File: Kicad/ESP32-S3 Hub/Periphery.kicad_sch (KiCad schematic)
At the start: 12 parts, among them SW1 Mitsumi R-667996, SW2 Mitsumi R-667996, SW3 DS04-254-2-04BK-SMT, U2 74HC595, U3 THVD1420DRLR

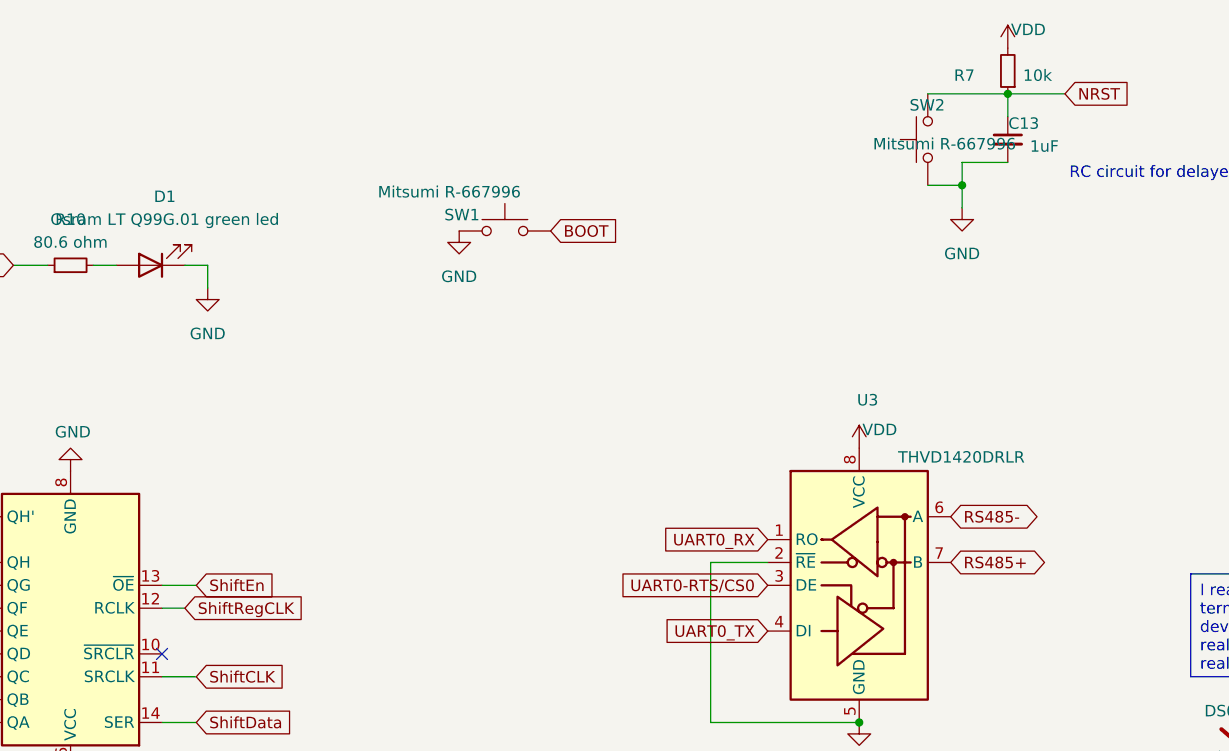
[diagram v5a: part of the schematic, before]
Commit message: Fixed OE pin by adding pullup, updated silkscreen
The silkscreen looks really nice now, I have all the port labels.
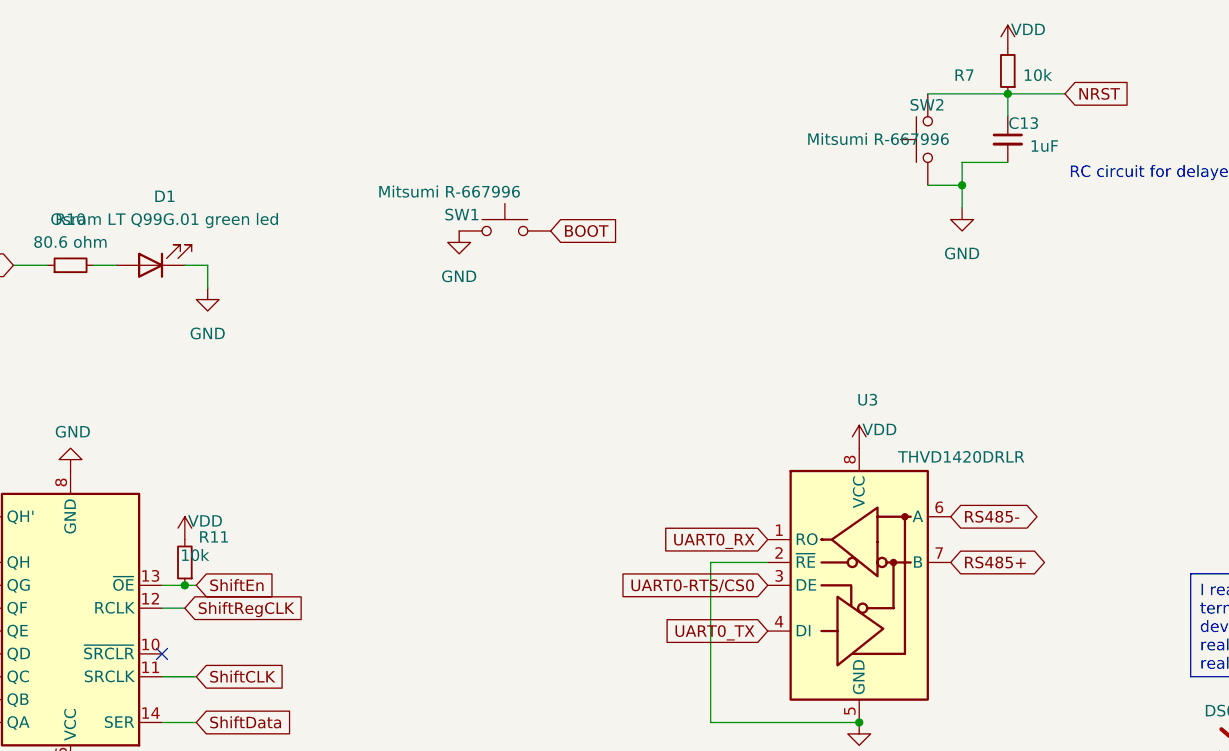
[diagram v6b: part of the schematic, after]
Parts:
- added R11: 10k, Resistor_SMD:R_0402_1005Metric, symbol Device:R_Small
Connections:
- net ShiftEn: now also R11.1
- net VDD: now also R11.2
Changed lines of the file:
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@@
+		(color 0 0 0 0)
+	)
+	(junction
+		(at 69.85 86.36)
+		(diameter 0)
 		(color 0 0 0 0)
 	)
@@
 	(wire
 		(pts
-			(xy 67.31 86.36) (xy 71.12 86.36)
+			(xy 67.31 86.36) (xy 69.85 86.36)
 		)
 		(stroke
@@
 		(pts
 			(xy 72.39 50.8) (xy 72.39 53.34)
+		)
+		(stroke
+			(width 0)
+			(type default)
+		)
+	)
+	(wire
+		(pts
+			(xy 69.85 86.36) (xy 71.12 86.36)
 		)
 		(stroke
@@
 		)
 		(property "Value" "Mitsumi R-667996"
-			(at 146.304 37.338 90)
+			(at 138.938 36.83 90)
 			(effects
 				(font
@@
 	(symbol
 		(lib_id "power:VDD")
+		(at 69.85 81.28 0)
+		(unit 1)
+		(exclude_from_sim no)
+		(in_bom yes)
+		(on_board yes)
+		(dnp no)
+		(property "Reference" "#PWR079"
+			(at 69.85 85.09 0)
+			(effects
+				(font
+					(size 1.27 1.27)
+				)
+				(hide yes)
+			)
+		)
+		(property "Value" "VDD"
+			(at 72.136 79.248 0)
+			(effects
+				(font
+					(size 1.27 1.27)
+				)
+			)
+		)
+		(property "Footprint" ""
+			(at 69.85 81.28 0)
+			(effects
+				(font
+					(size 1.27 1.27)
+				)
+				(hide yes)
+			)
+		)
+		(property "Datasheet" ""
+			(at 69.85 81.28 0)
+			(effects
+				(font
+					(size 1.27 1.27)
+				)
+				(hide yes)
+			)
+		)
+		(property "Description" "Power symbol creates a global label with name \"VDD\""
+			(at 69.85 81.28 0)
+			(effects
+				(font
+					(size 1.27 1.27)
+				)
+				(hide yes)
+			)
+		)
+		(pin "1"
+		)
+		(instances
+			(project "ESP32-S3 Hub"
+				(path "/a8c80fba-3bca-4358-b5bb-9ebf9383c658/c12991ca-4617-4c32-8678-9934d12b2f96"
+					(reference "#PWR079")
+					(unit 1)
+				)
+			)
+		)
+	)
+	(symbol
+		(lib_id "power:VDD")
 		(at 161.29 26.67 0)
 		(unit 1)
@@
 					(unit 1)
 				)
+			)
+		)
+	)
+	(symbol
+		(lib_id "Device:R_Small")
+		(at 69.85 83.82 180)
+		(unit 1)
+		(exclude_from_sim no)
+		(in_bom yes)
+		(on_board yes)
+		(dnp no)
+		(property "Reference" "R11"
+			(at 71.374 81.026 0)
+			(effects
+				(font
+					(size 1.27 1.27)
+				)
+				(justify right)
+			)
+		)
+		(property "Value" "10k"
+			(at 69.342 83.058 0)
+			(effects
+				(font
+					(size 1.27 1.27)
+				)
+				(justify right)
+			)
+		)
+		(property "Footprint" "Resistor_SMD:R_0402_1005Metric"
+			(at 69.85 83.82 0)
+			(effects
+				(font
+					(size 1.27 1.27)
+				)
+				(hide yes)
+			)
+		)
+		(property "Datasheet" "~"
+			(at 69.85 83.82 0)
+			(effects
+				(font
+					(size 1.27 1.27)
+				)
+				(hide yes)
+			)
+		)
+		(property "Description" "Resistor, small symbol"
+			(at 69.85 83.82 0)
+			(effects
+				(font
+					(size 1.27 1.27)
+				)
+				(hide yes)
+			)
+		)
+		(pin "1"
+		)
+		(pin "2"
+		)
+		(instances
+			(project "ESP32-S3 Hub"
+				(path "/a8c80fba-3bca-4358-b5bb-9ebf9383c658/c12991ca-4617-4c32-8678-9934d12b2f96"
+					(reference "R11")
+					(unit 1)
+				)

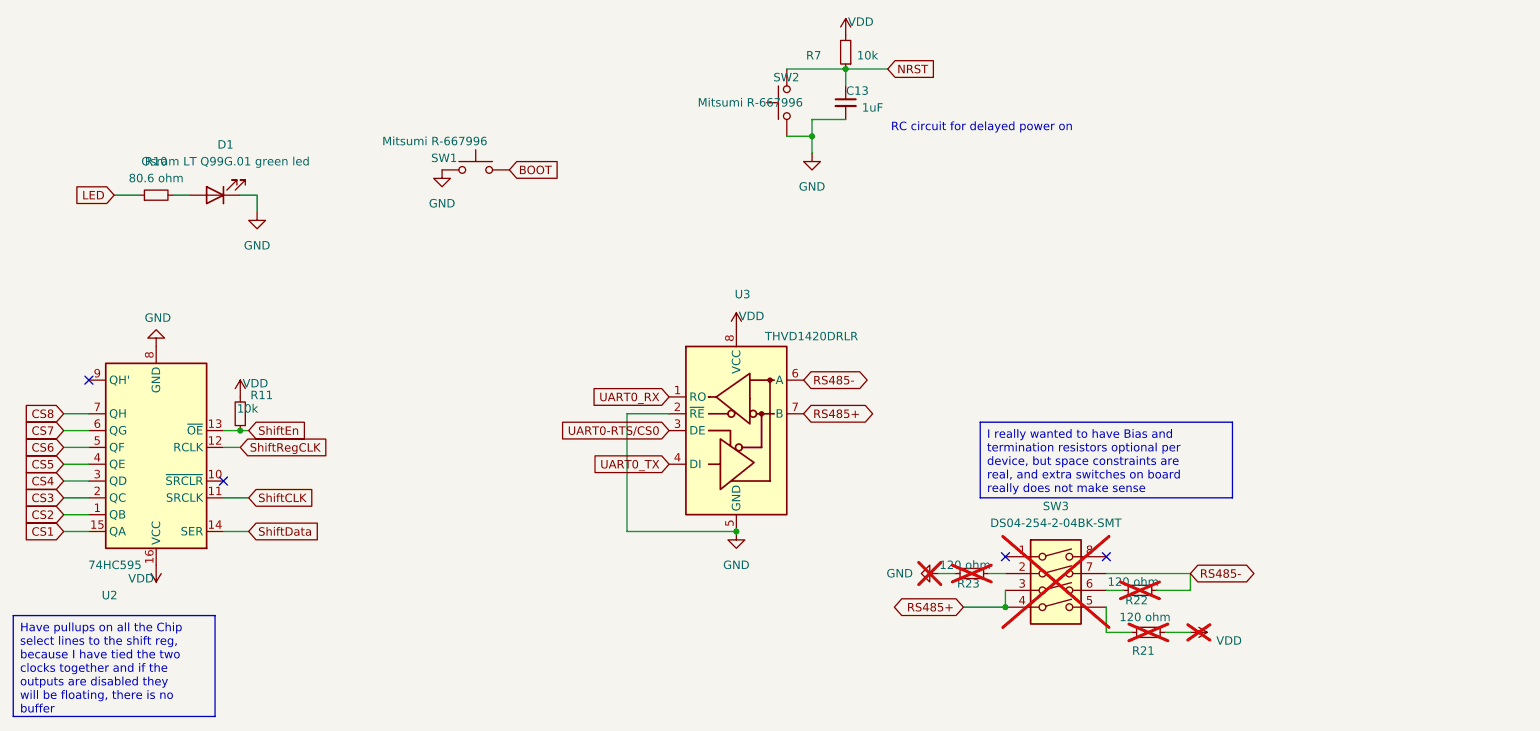
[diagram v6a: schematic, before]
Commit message: Added LCSC part numbers, DNP attr, and exported Gerbers
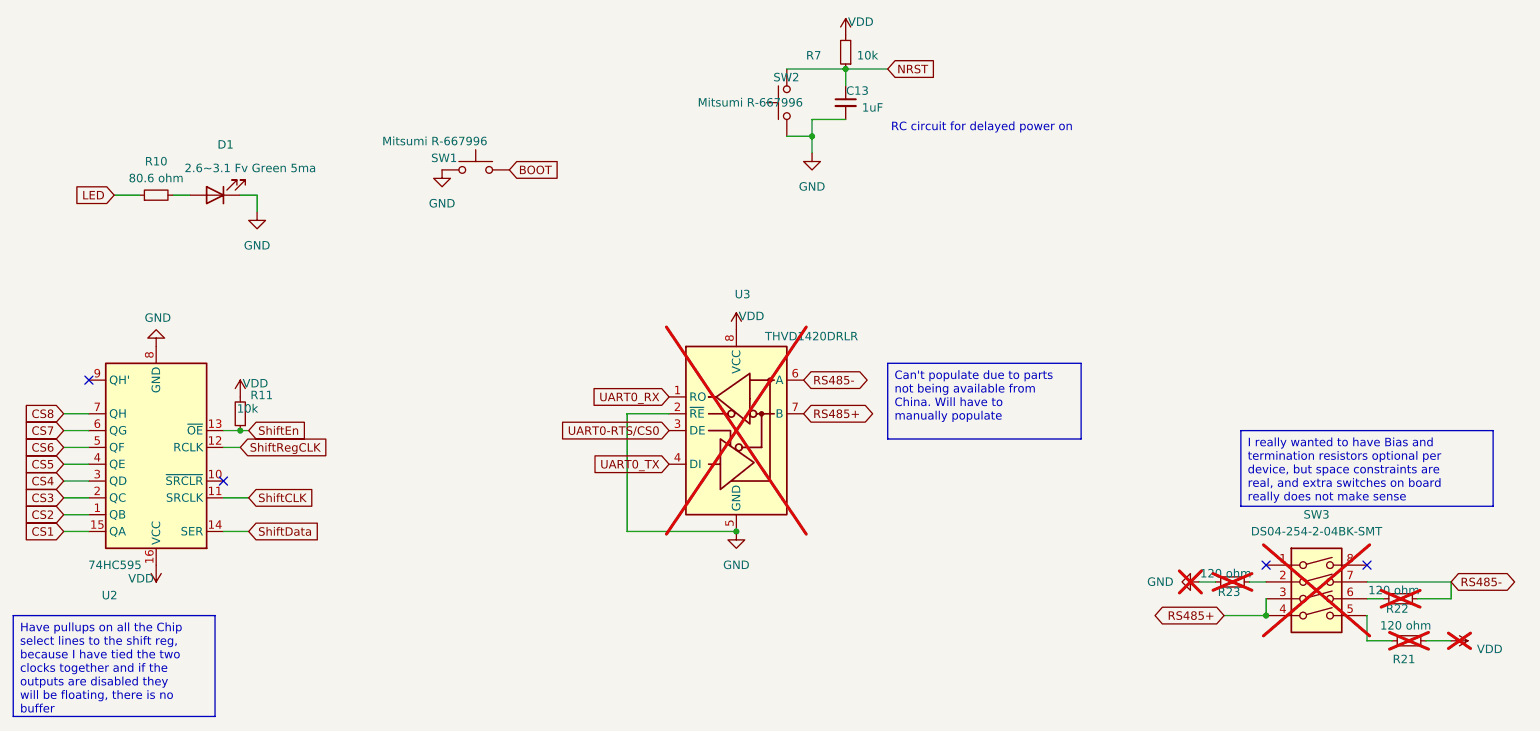
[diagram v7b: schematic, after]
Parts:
- C13: LCSC (none) -> C52923
- D1: value Osram LT Q99G.01 green led -> 2.6~3.1 Fv Green 5ma; LCSC (none) -> C3028858
- R10: LCSC (none) -> C185392
- R11, R7: LCSC (none) -> C25744
- SW1, SW2: LCSC (none) -> C4365007
- U2: LCSC (none) -> C730243
- U3: now not fitted
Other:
- moved on the sheet: R21, R22, R23, SW3
